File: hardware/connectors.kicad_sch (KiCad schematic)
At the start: 13 parts, among them J1 USB_C_Receptacle_USB2.0_16P, J2 Conn_01x04

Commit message: Update.
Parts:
- renumbered C9 to C11, C10 to C12, R12 to R10, R16 to R11, R17 to R12
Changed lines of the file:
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@@
 		(dnp no)
 		(fields_autoplaced yes)
-		(property "Reference" "C9"
+		(property "Reference" "C11"
 			(at 177.8 45.7199 0)
 			(effects
@@
 			(project ""
 				(path "/90430e5f-7049-4de8-b92d-f897c4a89819/7e2fbc03-0d09-4c94-a49f-ff5156ee2f2b"
-					(reference "C9")
+					(reference "C11")
 					(unit 1)
 				)
@@
 		(dnp no)
 		(fields_autoplaced yes)
-		(property "Reference" "R16"
+		(property "Reference" "R11"
 			(at 81.28 80.0099 0)
 			(effects
@@
 			(project "qw"
 				(path "/90430e5f-7049-4de8-b92d-f897c4a89819/7e2fbc03-0d09-4c94-a49f-ff5156ee2f2b"
-					(reference "R16")
+					(reference "R11")
 					(unit 1)
 				)
@@
 		(dnp no)
 		(fields_autoplaced yes)
-		(property "Reference" "R12"
+		(property "Reference" "R10"
 			(at 55.88 87.6299 0)
 			(effects
@@
 			(project ""
 				(path "/90430e5f-7049-4de8-b92d-f897c4a89819/7e2fbc03-0d09-4c94-a49f-ff5156ee2f2b"
-					(reference "R12")
+					(reference "R10")
 					(unit 1)
 				)
@@
 		(dnp no)
 		(fields_autoplaced yes)
-		(property "Reference" "R17"
+		(property "Reference" "R12"
 			(at 90.17 80.0099 0)
 			(effects
@@
 			(project "qw"
 				(path "/90430e5f-7049-4de8-b92d-f897c4a89819/7e2fbc03-0d09-4c94-a49f-ff5156ee2f2b"
-					(reference "R17")
+					(reference "R12")
 					(unit 1)
 				)
@@
 		(dnp no)
 		(fields_autoplaced yes)
-		(property "Reference" "C10"
+		(property "Reference" "C12"
 			(at 193.04 45.7199 0)
 			(effects
@@
 			(project "qw"
 				(path "/90430e5f-7049-4de8-b92d-f897c4a89819/7e2fbc03-0d09-4c94-a49f-ff5156ee2f2b"
-					(reference "C10")
-					(unit 1)
-				)
+					(reference "C12")
+					(unit 1)
+				)

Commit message: Update vias.
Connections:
- net 12V: now also J2.4 (Pin_4); no longer J2.2 (Pin_2)
- net GND: now also J2.2 (Pin_2); no longer J2.4 (Pin_4)
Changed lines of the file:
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@@
 	)
 	(junction
-		(at 212.09 43.18)
+		(at 212.09 41.91)
 		(diameter 0)
 		(color 0 0 0 0)
@@
 	(wire
 		(pts
+			(xy 199.39 45.72) (xy 212.09 45.72)
+		)
+		(stroke
+			(width 0)
+			(type default)
+		)
+	)
+	(wire
+		(pts
 			(xy 189.23 50.8) (xy 189.23 53.34)
 		)
@@
 	(wire
 		(pts
-			(xy 173.99 40.64) (xy 212.09 40.64)
-		)
-		(stroke
-			(width 0)
-			(type default)
-		)
-	)
-	(wire
-		(pts
 			(xy 77.47 57.15) (xy 83.82 57.15)
 		)
@@
 	(wire
 		(pts
+			(xy 212.09 41.91) (xy 212.09 43.18)
+		)
+		(stroke
+			(width 0)
+			(type default)
+		)
+	)
+	(wire
+		(pts
 			(xy 76.2 52.07) (xy 97.79 52.07)
 		)
@@
 	(wire
 		(pts
+			(xy 212.09 40.64) (xy 212.09 41.91)
+		)
+		(stroke
+			(width 0)
+			(type default)
+		)
+	)
+	(wire
+		(pts
 			(xy 173.99 53.34) (xy 173.99 50.8)
 		)
@@
 	(wire
 		(pts
-			(xy 212.09 43.18) (xy 212.09 45.72)
-		)
-		(stroke
-			(width 0)
-			(type default)
-		)
-	)
-	(wire
-		(pts
 			(xy 168.91 40.64) (xy 173.99 40.64)
 		)
@@
 	(wire
 		(pts
+			(xy 173.99 40.64) (xy 199.39 40.64)
+		)
+		(stroke
+			(width 0)
+			(type default)
+		)
+	)
+	(wire
+		(pts
+			(xy 208.28 41.91) (xy 212.09 41.91)
+		)
+		(stroke
+			(width 0)
+			(type default)
+		)
+	)
+	(wire
+		(pts
 			(xy 53.34 92.71) (xy 53.34 96.52)
 		)
@@
 	(wire
 		(pts
-			(xy 204.47 43.18) (xy 212.09 43.18)
+			(xy 199.39 40.64) (xy 199.39 45.72)
 		)
 		(stroke
@@
 	(hierarchical_label "GND"
 		(shape input)
+		(at 208.28 41.91 180)
+		(effects
+			(font
+				(size 1.27 1.27)
+			)
+			(justify right)
+		)
+	)
+	(hierarchical_label "GND"
+		(shape input)
 		(at 91.44 135.89 270)
 		(effects
@@
 		(effects
 			(font
-				(size 1.27 1.27)
-			)
-			(justify right)
-		)
-	)
-	(hierarchical_label "GND"
-		(shape output)
-		(at 204.47 43.18 180)
-		(effects
-			(font

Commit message: Add buttons.
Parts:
- J2: footprint TerminalBlock_Phoenix:TerminalBlock_Phoenix_MKDS-1,5-4-5.08_1x04_P5.08mm_Horizontal -> TerminalBlock_1x04_P5.08mm_SMD
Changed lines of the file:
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@@
 			)
 		)
-		(property "Footprint" "TerminalBlock_Phoenix:TerminalBlock_Phoenix_MKDS-1,5-4-5.08_1x04_P5.08mm_Horizontal"
+		(property "Footprint" "TerminalBlock_1x04_P5.08mm_SMD"
 			(at 217.17 40.64 0)
 			(effects

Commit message: Add HT psu.
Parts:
- added R16: 0, Resistor_SMD:R_1206_3216Metric, symbol Device:R
- J3: renamed from J2; footprint TerminalBlock_1x04_P5.08mm_SMD -> TerminalBlock:TerminalBlock_bornier-4_P5.08mm
- renumbered J1 to J2, R10 to R11, R11 to R12, R12 to R13, R13 to R14, R14 to R15
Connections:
- net 170V: now also R16.2; no longer C12.1, J3.1 (Pin_1)
- new net: C12.1, J3.1 (Pin_1), R16.1
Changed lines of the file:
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@@
+	)
+	(junction
+		(at 189.23 38.1)
+		(diameter 0)
+		(color 0 0 0 0)
 	)
 	(junction
@@
 	)
 	(junction
-		(at 189.23 38.1)
-		(diameter 0)
-		(color 0 0 0 0)
-	)
-	(junction
 		(at 77.47 62.23)
 		(diameter 0)
@@
 	(wire
 		(pts
+			(xy 185.42 38.1) (xy 189.23 38.1)
+		)
+		(stroke
+			(width 0)
+			(type default)
+		)
+	)
+	(wire
+		(pts
 			(xy 80.01 39.37) (xy 80.01 44.45)
 		)
@@
 	(wire
 		(pts
-			(xy 168.91 38.1) (xy 189.23 38.1)
-		)
-		(stroke
-			(width 0)
-			(type default)
-		)
-	)
-	(wire
-		(pts
 			(xy 76.2 49.53) (xy 87.63 49.53)
 		)
@@
 		(pts
 			(xy 189.23 38.1) (xy 212.09 38.1)
+		)
+		(stroke
+			(width 0)
+			(type default)
+		)
+	)
+	(wire
+		(pts
+			(xy 168.91 38.1) (xy 177.8 38.1)
 		)
 		(stroke
@@
 			)
 			(justify right)
+		)
+	)
+	(symbol
+		(lib_id "Device:R")
+		(at 181.61 38.1 270)
+		(unit 1)
+		(exclude_from_sim no)
+		(in_bom yes)
+		(on_board yes)
+		(dnp no)
+		(fields_autoplaced yes)
+		(property "Reference" "R16"
+			(at 181.61 31.75 90)
+			(effects
+				(font
+					(size 1.27 1.27)
+				)
+			)
+		)
+		(property "Value" "0"
+			(at 181.61 34.29 90)
+			(effects
+				(font
+					(size 1.27 1.27)
+				)
+			)
+		)
+		(property "Footprint" "Resistor_SMD:R_1206_3216Metric"
+			(at 181.61 36.322 90)
+			(effects
+				(font
+					(size 1.27 1.27)
+				)
+				(hide yes)
+			)
+		)
+		(property "Datasheet" "~"
+			(at 181.61 38.1 0)
+			(effects
+				(font
+					(size 1.27 1.27)
+				)
+				(hide yes)
+			)
+		)
+		(property "Description" "Resistor"
+			(at 181.61 38.1 0)
+			(effects
+				(font
+					(size 1.27 1.27)
+				)
+				(hide yes)
+			)
+		)
+		(pin "1"
+		)
+		(pin "2"
+		)
+		(instances
+			(project "nixie_clock"
+				(path "/90430e5f-7049-4de8-b92d-f897c4a89819/7e2fbc03-0d09-4c94-a49f-ff5156ee2f2b"
+					(reference "R16")
+					(unit 1)
+				)
+			)
 		)
 	)
@@
 		(dnp no)
 		(fields_autoplaced yes)
-		(property "Reference" "R13"
+		(property "Reference" "R14"
 			(at 91.44 43.18 90)
 			(effects
@@
 			(project ""
 				(path "/90430e5f-7049-4de8-b92d-f897c4a89819/7e2fbc03-0d09-4c94-a49f-ff5156ee2f2b"
-					(reference "R13")
+					(reference "R14")
 					(unit 1)
 				)
@@
 		(dnp no)
 		(fields_autoplaced yes)
-		(property "Reference" "J2"
+		(property "Reference" "J3"
 			(at 219.71 40.6399 0)
 			(effects
@@
 			)
 		)
-		(property "Footprint" "TerminalBlock_1x04_P5.08mm_SMD"
+		(property "Footprint" "TerminalBlock:TerminalBlock_bornier-4_P5.08mm"
 			(at 217.17 40.64 0)
 			(effects
@@
 			(project ""
 				(path "/90430e5f-7049-4de8-b92d-f897c4a89819/7e2fbc03-0d09-4c94-a49f-ff5156ee2f2b"
-					(reference "J2")
+					(reference "J3")
 					(unit 1)
 				)
@@
 		(dnp no)
 		(fields_autoplaced yes)
-		(property "Reference" "R11"
+		(property "Reference" "R12"
 			(at 81.28 80.0099 0)
 			(effects
@@
 			(project "qw"
 				(path "/90430e5f-7049-4de8-b92d-f897c4a89819/7e2fbc03-0d09-4c94-a49f-ff5156ee2f2b"
-					(reference "R11")
+					(reference "R12")
 					(unit 1)
 				)
@@
 		(dnp no)
 		(fields_autoplaced yes)
-		(property "Reference" "R10"
+		(property "Reference" "R11"
 			(at 55.88 87.6299 0)
 			(effects
@@
 			(project ""
 				(path "/90430e5f-7049-4de8-b92d-f897c4a89819/7e2fbc03-0d09-4c94-a49f-ff5156ee2f2b"
-					(reference "R10")
+					(reference "R11")
 					(unit 1)
 				)
@@
 		(dnp no)
 		(fields_autoplaced yes)
-		(property "Reference" "J1"
+		(property "Reference" "J2"
 			(at 60.96 36.83 0)
 			(effects
@@
 			(project ""
 				(path "/90430e5f-7049-4de8-b92d-f897c4a89819/7e2fbc03-0d09-4c94-a49f-ff5156ee2f2b"
-					(reference "J1")
+					(reference "J2")
 					(unit 1)
 				)
@@
 		(dnp no)
 		(fields_autoplaced yes)
-		(property "Reference" "R12"
+		(property "Reference" "R13"
 			(at 90.17 80.0099 0)
 			(effects
@@
 			(project "qw"
 				(path "/90430e5f-7049-4de8-b92d-f897c4a89819/7e2fbc03-0d09-4c94-a49f-ff5156ee2f2b"
-					(reference "R12")
+					(reference "R13")
 					(unit 1)
 				)
@@
 		(dnp no)
 		(fields_autoplaced yes)
-		(property "Reference" "R14"
+		(property "Reference" "R15"
 			(at 101.6 45.72 90)
 			(effects
@@
 			(project ""
 				(path "/90430e5f-7049-4de8-b92d-f897c4a89819/7e2fbc03-0d09-4c94-a49f-ff5156ee2f2b"
-					(reference "R14")
+					(reference "R15")
 					(unit 1)
 				)

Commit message: Update.
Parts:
- J3: footprint TerminalBlock:TerminalBlock_bornier-4_P5.08mm -> TerminalBlock_Phoenix:TerminalBlock_Phoenix_PT-1,5-4-3.5-H_1x04_P3.50mm_Horizontal
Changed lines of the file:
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@@
 			)
 		)
-		(property "Footprint" "TerminalBlock:TerminalBlock_bornier-4_P5.08mm"
+		(property "Footprint" "TerminalBlock_Phoenix:TerminalBlock_Phoenix_PT-1,5-4-3.5-H_1x04_P3.50mm_Horizontal"
 			(at 217.17 40.64 0)
 			(effects

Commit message: Add holes with via. Avoid too long tracks.
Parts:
- H1, H2, H3, H4: footprint MountingHole:MountingHole_3.2mm_M3_Pad -> MountingHole:MountingHole_3.2mm_M3_Pad_Via
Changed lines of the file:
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@@
 			)
 		)
-		(property "Footprint" "MountingHole:MountingHole_3.2mm_M3_Pad"
+		(property "Footprint" "MountingHole:MountingHole_3.2mm_M3_Pad_Via"
 			(at 104.14 127 0)
 			(effects
@@
 			)
 		)
-		(property "Footprint" "MountingHole:MountingHole_3.2mm_M3_Pad"
+		(property "Footprint" "MountingHole:MountingHole_3.2mm_M3_Pad_Via"
 			(at 76.2 127 0)
 			(effects
@@
 			)
 		)
-		(property "Footprint" "MountingHole:MountingHole_3.2mm_M3_Pad"
+		(property "Footprint" "MountingHole:MountingHole_3.2mm_M3_Pad_Via"
 			(at 127 127 0)
 			(effects
@@
 			)
 		)
-		(property "Footprint" "MountingHole:MountingHole_3.2mm_M3_Pad"
+		(property "Footprint" "MountingHole:MountingHole_3.2mm_M3_Pad_Via"
 			(at 45.72 127 0)
 			(effects

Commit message: Change power connector.
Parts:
- J3: value Conn_01x04 -> Conn_01x03; footprint TerminalBlock_Phoenix:TerminalBlock_Phoenix_PT-1,5-4-3.5-H_1x04_P3.50mm_Horizontal -> TerminalBlock_Phoenix:TerminalBlock_Phoenix_PT-1,5-3-3.5-H_1x03_P3.50mm_Horizontal; symbol Connector_Generic:Conn_01x04 -> Connector_Generic:Conn_01x03
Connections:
- net 12V: now also J3.3 (Pin_3); no longer J3.4 (Pin_4)
- net GND: no longer J3.3 (Pin_3)
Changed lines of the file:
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@@
-	)
-	(junction
-		(at 212.09 41.91)
-		(diameter 0)
-		(color 0 0 0 0)
 	)
 	(junction
@@
 	(wire
 		(pts
-			(xy 199.39 45.72) (xy 212.09 45.72)
+			(xy 199.39 43.18) (xy 212.09 43.18)
 		)
 		(stroke
@@
 	(wire
 		(pts
-			(xy 212.09 41.91) (xy 212.09 43.18)
-		)
-		(stroke
-			(width 0)
-			(type default)
-		)
-	)
-	(wire
-		(pts
 			(xy 76.2 52.07) (xy 97.79 52.07)
 		)
@@
 	(wire
 		(pts
+			(xy 212.09 40.64) (xy 208.28 40.64)
+		)
+		(stroke
+			(width 0)
+			(type default)
+		)
+	)
+	(wire
+		(pts
 			(xy 91.44 129.54) (xy 104.14 129.54)
 		)
@@
 	(wire
 		(pts
-			(xy 212.09 40.64) (xy 212.09 41.91)
-		)
-		(stroke
-			(width 0)
-			(type default)
-		)
-	)
-	(wire
-		(pts
 			(xy 173.99 53.34) (xy 173.99 50.8)
 		)
@@
 	(wire
 		(pts
-			(xy 208.28 41.91) (xy 212.09 41.91)
-		)
-		(stroke
-			(width 0)
-			(type default)
-		)
-	)
-	(wire
-		(pts
 			(xy 53.34 92.71) (xy 53.34 96.52)
 		)
@@
 	(wire
 		(pts
-			(xy 199.39 40.64) (xy 199.39 45.72)
+			(xy 199.39 40.64) (xy 199.39 43.18)
 		)
 		(stroke
@@
 	(hierarchical_label "GND"
 		(shape input)
-		(at 208.28 41.91 180)
+		(at 208.28 40.64 180)
 		(effects
 			(font
@@
 	)
 	(symbol
-		(lib_id "Connector_Generic:Conn_01x04")
+		(lib_id "Connector_Generic:Conn_01x03")
 		(at 217.17 40.64 0)
 		(unit 1)
@@
 		(fields_autoplaced yes)
 		(property "Reference" "J3"
-			(at 219.71 40.6399 0)
+			(at 219.71 39.3699 0)
 			(effects
 				(font
@@
 			)
 		)
-		(property "Value" "Conn_01x04"
-			(at 219.71 43.1799 0)
+		(property "Value" "Conn_01x03"
+			(at 219.71 41.9099 0)
 			(effects
 				(font
@@
 			)
 		)
-		(property "Footprint" "TerminalBlock_Phoenix:TerminalBlock_Phoenix_PT-1,5-4-3.5-H_1x04_P3.50mm_Horizontal"
+		(property "Footprint" "TerminalBlock_Phoenix:TerminalBlock_Phoenix_PT-1,5-3-3.5-H_1x03_P3.50mm_Horizontal"
 			(at 217.17 40.64 0)
 			(effects
@@
 			)
 		)
-		(property "Description" "Generic connector, single row, 01x04, script generated (kicad-library-utils/schlib/autogen/connector/)"
+		(property "Description" "Generic connector, single row, 01x03, script generated (kicad-library-utils/schlib/autogen/connector/)"
 			(at 217.17 40.64 0)
 			(effects
@@
 		(pin "3"
 		)
-		(pin "4"
-		)
 		(instances

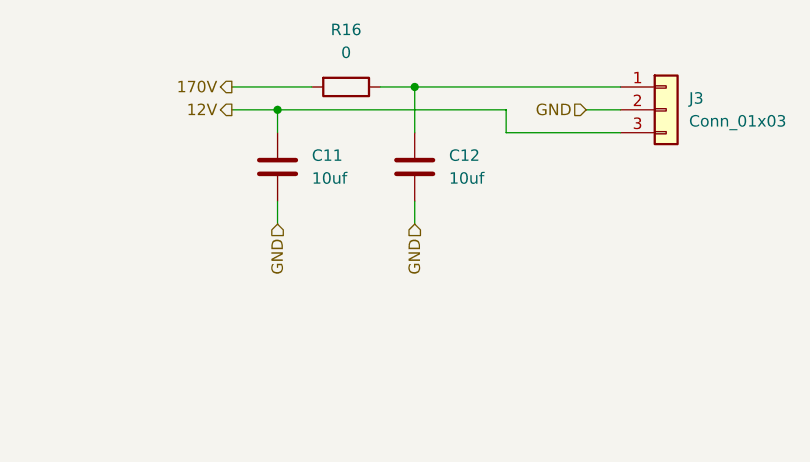
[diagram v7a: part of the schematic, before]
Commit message: Rework  3.3v power supply (fix error on fb loop). Put 1206 back on HV part.
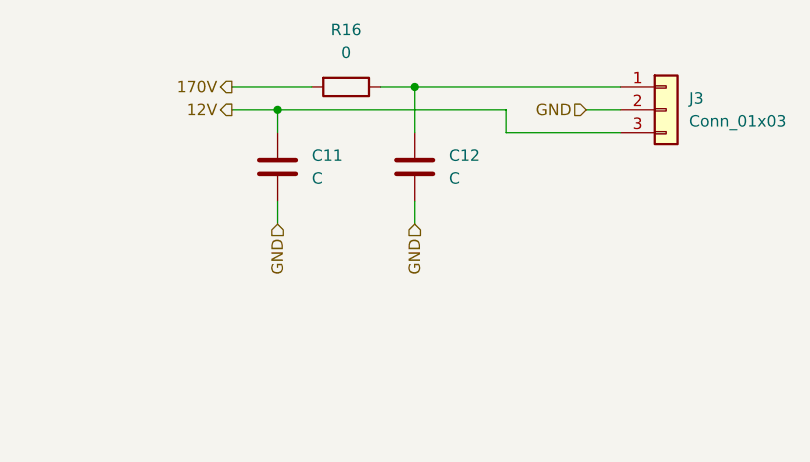
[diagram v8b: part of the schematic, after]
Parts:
- C11, C12: value 10uf -> C
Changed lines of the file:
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@@
 			)
 		)
-		(property "Value" "10uf"
+		(property "Value" "C"
 			(at 177.8 48.2599 0)
 			(effects
@@
 			)
 		)
-		(property "Value" "10uf"
+		(property "Value" "C"
 			(at 193.04 48.2599 0)
 			(effects
